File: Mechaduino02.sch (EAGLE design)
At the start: 64 parts, among them IC1 SAMD21G18A-AUT, Q1 BSS138, Q2 NFET, Q3 BSS138, Q4 BSS138, Q5 BSS138, U1 TLV70233PDBVR, Y1 32,768Khz

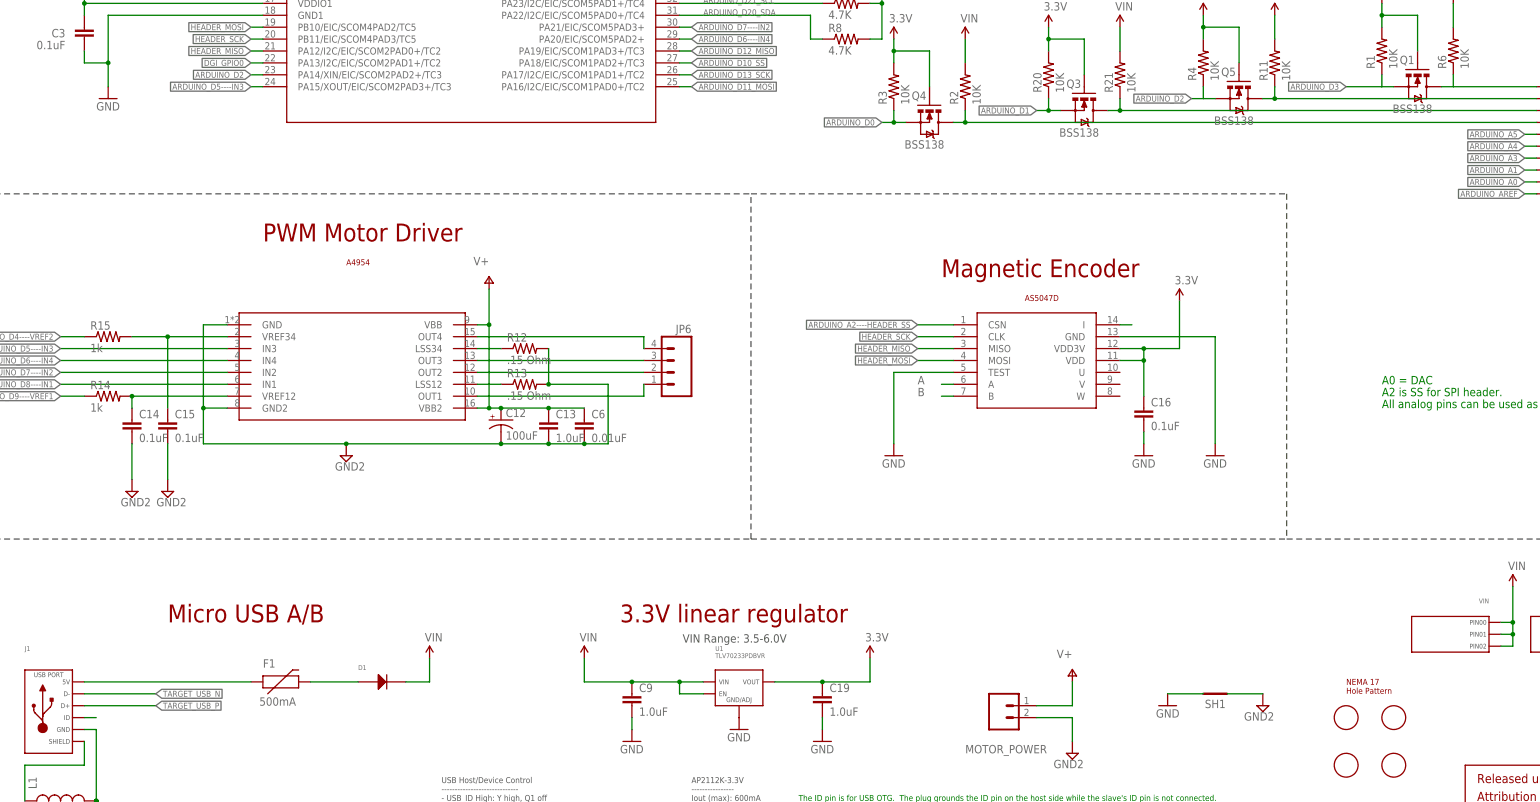
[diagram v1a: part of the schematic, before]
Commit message: fixed xtal caps and power caps to 0603
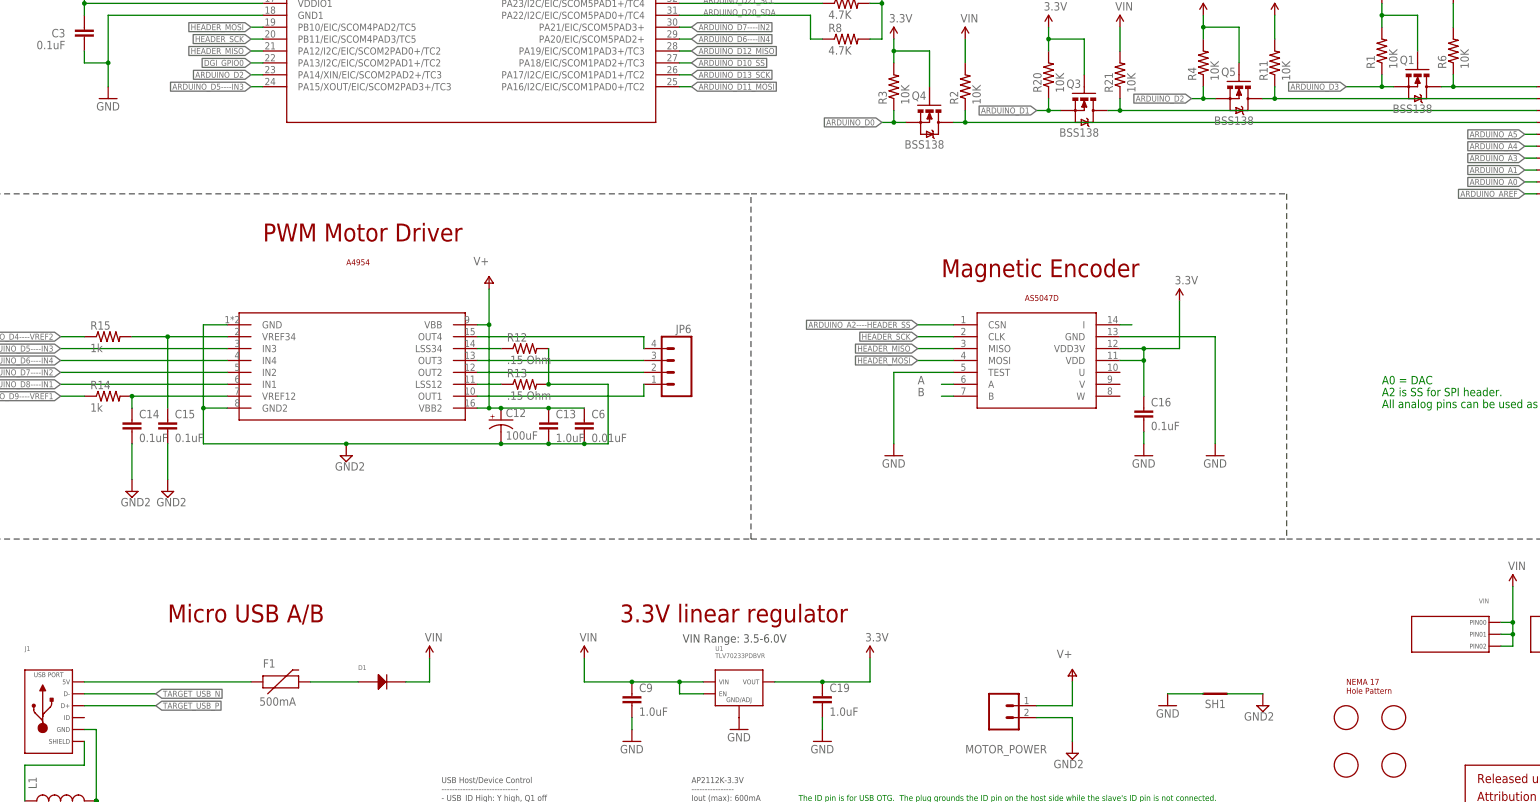
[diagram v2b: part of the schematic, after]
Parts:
- C6, C7, C8: device swift:CAP0402 -> swift:CAP0603
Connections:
- removed net N$7: J1.ID
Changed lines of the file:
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@@
 <part name="C5" library="swift" deviceset="CAP" device="0402" value="0.1uF"/>
 <part name="GND41" library="PowerTags" deviceset="GND" device=""/>
-<part name="C7" library="swift" deviceset="CAP" device="0402" value="18pF"/>
-<part name="C8" library="swift" deviceset="CAP" device="0402" value="18pF"/>
+<part name="C7" library="swift" deviceset="CAP" device="0603" value="18pF"/>
+<part name="C8" library="swift" deviceset="CAP" device="0603" value="18pF"/>
 <part name="LED1" library="Opto" deviceset="0044_KPT-2012YC" device="" value="Green"/>
 <part name="R7" library="adafruit" deviceset="R-US_" device="R0402-VISHAY" value="4.7K"/>
@@
 <part name="R20" library="adafruit" deviceset="R-US_" device="R0402-VISHAY" value="10K"/>
 <part name="R21" library="adafruit" deviceset="R-US_" device="R0402-VISHAY" value="10K"/>
-<part name="C6" library="swift" deviceset="CAP" device="0402" value="0.01uF"/>
+<part name="C6" library="swift" deviceset="CAP" device="0603" value="0.01uF"/>
 <part name="C19" library="swift" deviceset="CAP" device="0402" value="1.0uF"/>
 <part name="GND8" library="supply1" deviceset="GND" device=""/>
@@
 <pinref part="Q1" gate="G$1" pin="S"/>
 <wire x1="317.5" y1="182.88" x2="314.96" y2="182.88" width="0.1524" layer="91"/>
+<junction x="314.96" y="182.88"/>
 </segment>
 </net>
@@
 <pinref part="Q5" gate="G$1" pin="S"/>
 <wire x1="276.86" y1="180.34" x2="279.4" y2="180.34" width="0.1524" layer="91"/>
+<junction x="276.86" y="180.34"/>
 </segment>
 </net>
@@
 <pinref part="SUPPLY1" gate="G$1" pin="VIN"/>
 <pinref part="R6" gate="G$1" pin="2"/>
-</segment>
-</net>
-<net name="N$7" class="0">
-<segment>
-<wire x1="38.1" y1="48.26" x2="40.64" y2="48.26" width="0.1524" layer="91"/>
-<pinref part="J1" gate="G$1" pin="ID"/>
 </segment>
 </net>
@@
 <pinref part="J2" gate="G$1" pin="PIN0"/>
 <wire x1="330.2" y1="182.88" x2="347.98" y2="182.88" width="0.1524" layer="91"/>
-</segment>
-</net>
+<junction x="330.2" y="182.88"/>
+</segment>
+</net>

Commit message: a couple more changes
fixed cap sizes?  changed some text under regulator
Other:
- note added: "VIN: 5V (3.3V is ok if USB is not plugged in.)"
- note removed: "VIN Range: 3.5-6.0V"
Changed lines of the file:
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@@
 <?xml version="1.0" encoding="utf-8"?>
 <!DOCTYPE eagle SYSTEM "eagle.dtd">
-<eagle version="7.7.0">
+<eagle version="7.3.0">
 <drawing>
 <settings>
@@
 <grid distance="0.1" unitdist="inch" unit="inch" style="lines" multiple="1" display="no" altdistance="0.01" altunitdist="inch" altunit="inch"/>
 <layers>
-<layer number="1" name="Top" color="4" fill="1" visible="yes" active="no"/>
-<layer number="16" name="Bottom" color="1" fill="1" visible="yes" active="no"/>
-<layer number="17" name="Pads" color="2" fill="1" visible="yes" active="no"/>
-<layer number="18" name="Vias" color="2" fill="1" visible="yes" active="no"/>
-<layer number="19" name="Unrouted" color="15" fill="1" visible="yes" active="no"/>
-<layer number="20" name="Dimension" color="15" fill="1" visible="yes" active="no"/>
-<layer number="21" name="tPlace" color="7" fill="1" visible="yes" active="no"/>
-<layer number="22" name="bPlace" color="15" fill="1" visible="yes" active="no"/>
-<layer number="23" name="tOrigins" color="15" fill="1" visible="yes" active="no"/>
-<layer number="24" name="bOrigins" color="15" fill="1" visible="yes" active="no"/>
-<layer number="25" name="tNames" color="10" fill="1" visible="yes" active="no"/>
-<layer number="26" name="bNames" color="7" fill="1" visible="yes" active="no"/>
-<layer number="27" name="tValues" color="7" fill="1" visible="yes" active="no"/>
-<layer number="28" name="bValues" color="7" fill="1" visible="yes" active="no"/>
+<layer number="1" name="Top" color="4" fill="1" visible="no" active="no"/>
+<layer number="16" name="Bottom" color="1" fill="1" visible="no" active="no"/>
+<layer number="17" name="Pads" color="2" fill="1" visible="no" active="no"/>
+<layer number="18" name="Vias" color="2" fill="1" visible="no" active="no"/>
+<layer number="19" name="Unrouted" color="15" fill="1" visible="no" active="no"/>
+<layer number="20" name="Dimension" color="15" fill="1" visible="no" active="no"/>
+<layer number="21" name="tPlace" color="7" fill="1" visible="no" active="no"/>
+<layer number="22" name="bPlace" color="15" fill="1" visible="no" active="no"/>
+<layer number="23" name="tOrigins" color="15" fill="1" visible="no" active="no"/>
+<layer number="24" name="bOrigins" color="15" fill="1" visible="no" active="no"/>
+<layer number="25" name="tNames" color="10" fill="1" visible="no" active="no"/>
+<layer number="26" name="bNames" color="7" fill="1" visible="no" active="no"/>
+<layer number="27" name="tValues" color="7" fill="1" visible="no" active="no"/>
+<layer number="28" name="bValues" color="7" fill="1" visible="no" active="no"/>
 <layer number="29" name="tStop" color="7" fill="3" visible="no" active="no"/>
 <layer number="30" name="bStop" color="7" fill="6" visible="no" active="no"/>
@@
 <layer number="35" name="tGlue" color="7" fill="4" visible="no" active="no"/>
 <layer number="36" name="bGlue" color="7" fill="5" visible="no" active="no"/>
-<layer number="37" name="tTest" color="7" fill="1" visible="yes" active="no"/>
-<layer number="38" name="bTest" color="7" fill="1" visible="yes" active="no"/>
+<layer number="37" name="tTest" color="7" fill="1" visible="no" active="no"/>
+<layer number="38" name="bTest" color="7" fill="1" visible="no" active="no"/>
 <layer number="39" name="tKeepout" color="4" fill="11" visible="no" active="no"/>
 <layer number="40" name="bKeepout" color="1" fill="11" visible="no" active="no"/>
@@
 <layer number="44" name="Drills" color="7" fill="1" visible="no" active="no"/>
 <layer number="45" name="Holes" color="7" fill="1" visible="no" active="no"/>
-<layer number="46" name="Milling" color="3" fill="1" visible="yes" active="no"/>
-<layer number="47" name="Measures" color="7" fill="1" visible="yes" active="no"/>
-<layer number="48" name="Document" color="7" fill="1" visible="yes" active="no"/>
-<layer number="49" name="Reference" color="7" fill="1" visible="yes" active="no"/>
-<layer number="50" name="dxf" color="12" fill="1" visible="yes" active="no"/>
-<layer number="51" name="tDocu" color="7" fill="1" visible="yes" active="no"/>
-<layer number="52" name="bDocu" color="7" fill="1" visible="yes" active="no"/>
-<layer number="53" name="tGND_GNDA" color="7" fill="1" visible="yes" active="no"/>
-<layer number="54" name="bGND_GNDA" color="7" fill="1" visible="yes" active="no"/>
-<layer number="56" name="wert" color="7" fill="1" visible="yes" active="no"/>
-<layer number="57" name="tCAD" color="7" fill="1" visible="yes" active="no"/>
-<layer number="59" name="tCarbon" color="7" fill="1" visible="yes" active="no"/>
-<layer number="60" name="bCarbon" color="7" fill="1" visible="yes" active="no"/>
+<layer number="46" name="Milling" color="3" fill="1" visible="no" active="no"/>
+<layer number="47" name="Measures" color="7" fill="1" visible="no" active="no"/>
+<layer number="48" name="Document" color="7" fill="1" visible="no" active="no"/>
+<layer number="49" name="Reference" color="7" fill="1" visible="no" active="no"/>
+<layer number="50" name="dxf" color="12" fill="1" visible="no" active="no"/>
+<layer number="51" name="tDocu" color="7" fill="1" visible="no" active="no"/>
+<layer number="52" name="bDocu" color="7" fill="1" visible="no" active="no"/>
+<layer number="53" name="tGND_GNDA" color="7" fill="1" visible="no" active="no"/>
+<layer number="54" name="bGND_GNDA" color="7" fill="1" visible="no" active="no"/>
+<layer number="56" name="wert" color="7" fill="1" visible="no" active="no"/>
+<layer number="57" name="tCAD" color="7" fill="1" visible="no" active="no"/>
+<layer number="59" name="tCarbon" color="7" fill="1" visible="no" active="no"/>
+<layer number="60" name="bCarbon" color="7" fill="1" visible="no" active="no"/>
 <layer number="90" name="Modules" color="5" fill="1" visible="yes" active="yes"/>
 <layer number="91" name="Nets" color="2" fill="1" visible="yes" active="yes"/>
@@
 <text x="111.76" y="269.24" size="3.81" layer="94">SAMD21</text>
 <text x="76.2" y="149.86" size="3.81" layer="94">PWM Motor Driver</text>
-<text x="187.96" y="66.04" size="1.778" layer="97" rot="R180">VIN Range: 3.5-6.0V</text>
+<text x="200.66" y="66.04" size="1.778" layer="97" rot="R180">VIN: 5V (3.3V is ok if USB is not plugged in.)</text>
 <text x="167.64" y="35.56" size="1.27" layer="97" align="top-left">AP2112K-3.3V
 ----------------

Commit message: updated schematic text
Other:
- note added: "Micro USB"
- note added: "TLV70233PDBVR ---------------- Iout (max): 300mA Vin (max): 6.0V Vdo (typ): 220mV Iq: 35uA"
- note added: "Use VOUT or the 3V3 pins to power external modules."
- note removed: "AP2112K-3.3V ---------------- Iout (max): 600mA Vin (max): 6.5V Vdrop (max): 250mV Iq: 55uA"
- note removed: "Micro USB A/B"
- note removed: "Resistor R10 limits current if host pin goes high while USB ID pin is low."
- note removed: "So if the A end of a USB OTG cable is inserted into the USB connector, Q1 allows power to flow from VIN to the USB device."
- note removed: "The ID pin is for USB OTG. The plug grounds the ID pin on the host side while the slave's ID pin is not connected."
- note removed: "The inverter then pulls the enable pin on the load switch high."
- note removed: "USB Host/Device Control ----------------------------- - USB_ID High: Y high, Q1 off - USB_ID Low: Y low, Q1 on - Set USB_HOST_EN low to turn Q1 on and route power OUT the board. - USB_HOST_EN floating or HIGH turns Q1 off. USB supply flows through Q1 body diode."
- note removed: "Use VOUT or the 3V3 pin to power external modules."
- note removed: "When enabling host mode, the USB_HOST_EN pin goes low."
- note removed: "When in host mode it is necessary for you to supply 5V to VIN."
- moved on the sheet: 3V3, C12, C13, C14, C15, C16, C19, C6, C9, D1, F1, GND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
